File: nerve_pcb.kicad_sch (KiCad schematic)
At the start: 48 parts, among them J1 TC2050-IDC, J2 2171750001, J4 472192001, J5 2x8, J6 2x15, SW1 SPST, SW2 SPST, U1 ld39150dt33-r, U2 STM32F446RET, Y1 8M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

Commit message: Schematic corrections
- Add decoupling caps for sensor ICs
- Fix clock circuits
- Add BNO085 clock jumper
- Minor cleanup
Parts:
- removed Y1: 8M, common:xtal_abm3b-8.000mhz-10-1-u-t, symbol common:abm3b-8.000mhz-10-1-u-t
- removed Y2: 32k768, common:xtal_abs25-32.768khz-6-t, symbol common:abs25-32.768khz-6-t
- added Y1: 8M, common:ecs_ecx-64, symbol common:ecs-80-18-23b-jtn-tr_8mhz
- added Y2: 32k768, common:ecs_ecx-34r, symbol common:ecs-_327-12_5-34r-c-tr_32k768hz
- C12, C13: value 20p -> 26p
- C15, C16: value 1p5 -> 15p
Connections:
- net GND: now also Y1.2, Y1.4
- net GPIO_IMU_P0: now also U2.50 (PA15); no longer U2.40 (PC9)
- net GPIO_IMU_RST: now also U2.40 (PC9); no longer U2.50 (PA15)
- net HSE_OUT: now also Y1.3
- net at C12.1, R11.2: now also Y1.1
- net at C15.1, R12.2: now also Y2.1
- net at C16.1, R13.2: now also Y2.2
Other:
- moved on the sheet: C12, C13, C15, C16, R11

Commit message: Major stackup revision and cleanup
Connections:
- net USART1_RX: now also J6.12 (Pin_12); no longer J6.10 (Pin_10)
- net USART1_TX: now also J6.10 (Pin_10); no longer J6.12 (Pin_12)

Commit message: Fix HSE clock caps
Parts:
- C12, C13: value 26p -> 30p
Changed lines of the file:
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@@
 			)
 		)
-		(property "Value" "26p"
+		(property "Value" "30p"
 			(at 40.64 109.22 0)
 			(effects
@@
 			)
 		)
-		(property "Value" "26p"
+		(property "Value" "30p"
 			(at 22.86 109.22 0)
 			(effects

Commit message: Simplify clock circuits
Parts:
- removed R11, R12, R13: 0R, Resistor_SMD:R_0603_1608Metric, symbol Device:R
- C12, C13: footprint Capacitor_SMD:C_0603_1608Metric -> Capacitor_SMD:C_0402_1005Metric
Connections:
- net HSE_IN: now also C12.1, Y1.1
- net LSE_IN: now also C15.1, Y2.1
- net LSE_OUT: now also C16.1, Y2.2
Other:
- moved on the sheet: C15, C16, Y2

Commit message: Swap 32k768 crystal caps to 18pF
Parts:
- C15, C16: value 15p -> 18p
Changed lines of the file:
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@@
 			)
 		)
-		(property "Value" "15p"
+		(property "Value" "18p"
 			(at 22.86 153.67 0)
 			(effects
@@
 			)
 		)
-		(property "Value" "15p"
+		(property "Value" "18p"
 			(at 40.64 153.67 0)
 			(effects

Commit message: Update J5 2x8 GPS connector
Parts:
- removed J5: 2x8, Connector_PinSocket_1.27mm:PinSocket_2x08_P1.27mm_Vertical_SMD, symbol Connector_Generic:Conn_02x08_Odd_Even
- added J5: BF030-16A-B1-0360-0277-0600-LB, connectors:bf030-16a-b1-0360-0277-0600-lb, symbol connectors:bf030-16a-b1-0360-0277-0600-lb
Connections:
- net +3.3VBATT: now also J5.13
- net +3V3: now also J5.3, J5.4
- net +5V: now also J5.1, J5.2
- net GND: now also J5.12, J5.9
- net GPIO_GPS_RST: now also J5.11
- net PC1: now also J5.6
- net PC2: now also J5.8
- net PC3: now also J5.10
- net TIM1_CH1_PWM: now also J5.14
- net USART2_RX: now also J5.5
- net USART2_TX: now also J5.7
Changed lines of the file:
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@@
-	)
-	(symbol
-		(lib_id "Connector_Generic:Conn_02x08_Odd_Even")
-		(at 195.58 129.54 0)
-		(unit 1)
-		(exclude_from_sim no)
-		(in_bom yes)
-		(on_board yes)
-		(dnp no)
-		(fields_autoplaced yes)
-		(property "Reference" "J5"
-			(at 196.85 115.57 0)
-			(effects
-				(font
-					(size 1.27 1.27)
-				)
-			)
-		)
-		(property "Value" "2x8"
-			(at 196.85 118.11 0)
-			(effects
-				(font
-					(size 1.27 1.27)
-				)
-			)
-		)
-		(property "Footprint" "Connector_PinSocket_1.27mm:PinSocket_2x08_P1.27mm_Vertical_SMD"
-			(at 195.58 129.54 0)
-			(effects
-				(font
-					(size 1.27 1.27)
-				)
-				(hide yes)
-			)
-		)
-		(property "Datasheet" "~"
-			(at 195.58 129.54 0)
-			(effects
-				(font
-					(size 1.27 1.27)
-				)
-				(hide yes)
-			)
-		)
-		(property "Description" "Generic connector, double row, 02x08, odd/even pin numbering scheme (row 1 odd numbers, row 2 even numbers), script generated (kicad-library-utils/schlib/autogen/connector/)"
-			(at 195.58 129.54 0)
-			(effects
-				(font
-					(size 1.27 1.27)
-				)
-				(hide yes)
-			)
-		)
-		(pin "1"
-		)
-		(pin "3"
-		)
-		(pin "7"
-		)
-		(pin "4"
-		)
-		(pin "13"
-		)
-		(pin "14"
-		)
-		(pin "2"
-		)
-		(pin "10"
-		)
-		(pin "6"
-		)
-		(pin "8"
-		)
-		(pin "15"
-		)
-		(pin "11"
-		)
-		(pin "12"
-		)
-		(pin "9"
-		)
-		(pin "5"
-		)
-		(pin "16"
-		)
-		(instances
-			(project ""
-				(path "/c0277862-b3f2-4e0e-986f-34702f0543f0"
-					(reference "J5")
-					(unit 1)
-				)
-			)
-		)
 	)
 	(symbol
@@
 					(unit 1)
 				)
+			)
+		)
+	)
+	(symbol
+		(lib_id "connectors:bf030-16a-b1-0360-0277-0600-lb")
+		(at 196.85 130.81 0)
+		(unit 1)
+		(exclude_from_sim no)
+		(in_bom yes)
+		(on_board yes)
+		(dnp no)
+		(property "Reference" "J5"
+			(at 196.85 119.38 0)
+			(effects
+				(font
+					(size 1.27 1.27)
+				)
+			)
+		)
+		(property "Value" "BF030-16A-B1-0360-0277-0600-LB"
+			(at 196.85 147.32 0)
+			(effects
+				(font
+					(size 1.27 1.27)
+				)
+				(hide yes)
+			)
+		)
+		(property "Footprint" "connectors:bf030-16a-b1-0360-0277-0600-lb"
+			(at 196.85 130.81 0)
+			(effects
+				(font
+					(size 1.27 1.27)
+				)
+				(hide yes)
+			)
+		)
+		(property "Datasheet" "https://gct.co/files/drawings/bf030.pdf"
+			(at 196.85 130.81 0)
+			(effects
+				(font
+					(size 1.27 1.27)
+				)
+				(hide yes)
+			)
+		)
+		(property "Description" "Connector Header Surface Mount 16 position 0.079\" (2.00mm)"
+			(at 196.85 130.81 0)
+			(effects
+				(font
+					(size 1.27 1.27)
+				)
+				(hide yes)
+			)
+		)
+		(property "Manufacturer" "GCT"
+			(at 196.85 130.81 0)
+			(effects
+				(font
+					(size 1.27 1.27)
+				)
+				(hide yes)
+			)
+		)
+		(property "Manufacturer Part Number" "BF030-16A-B1-0360-0277-0600-LB"
+			(at 196.85 130.81 0)
+			(effects
+				(font
+					(size 1.27 1.27)
+				)
+				(hide yes)
+			)
+		)
+		(property "Distributor" "DigiKey"
+			(at 196.85 130.81 0)
+			(effects
+				(font
+					(size 1.27 1.27)
+				)
+				(hide yes)
+			)
+		)
+		(property "Distributor Part Number" "2073-BF030-16A-B1-0360-0277-0600-LBCT-ND"
+			(at 196.85 130.81 0)
+			(effects
+				(font
+					(size 1.27 1.27)
+				)
+				(hide yes)
+			)
+		)
+		(property "Distributor Link" "https://www.digikey.ca/en/products/detail/gct/BF030-16A-B1-0360-0277-0600-LB/16397007"
+			(at 196.85 130.81 0)
+			(effects
+				(font
+					(size 1.27 1.27)
+				)
+				(hide yes)
+			)
+		)
+		(pin "4"
+		)
+		(pin "9"
+		)
+		(pin "13"
+		)
+		(pin "10"
+		)
+		(pin "16"
+		)
+		(pin "8"
+		)
+		(pin "12"
+		)
+		(pin "2"
+		)
+		(pin "7"
+		)
+		(pin "1"
+		)
+		(pin "6"
+		)
+		(pin "15"
+		)
+		(pin "3"
+		)
+		(pin "5"
+		)
+		(pin "11"
+		)
+		(pin "14"
+		)
+		(instances
+			(project ""
+				(path "/c0277862-b3f2-4e0e-986f-34702f0543f0"
+					(reference "J5")
+					(unit 1)
+				)

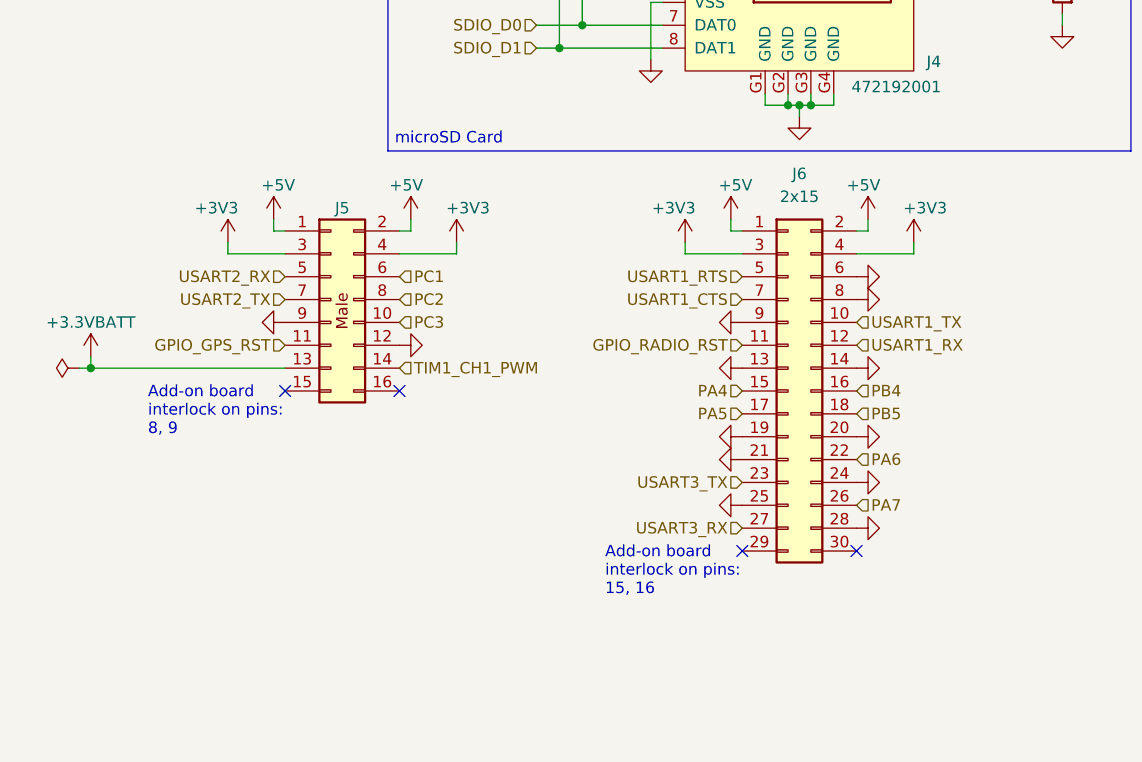
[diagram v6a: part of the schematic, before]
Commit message: Cleanup and update 2x10 Radio connector
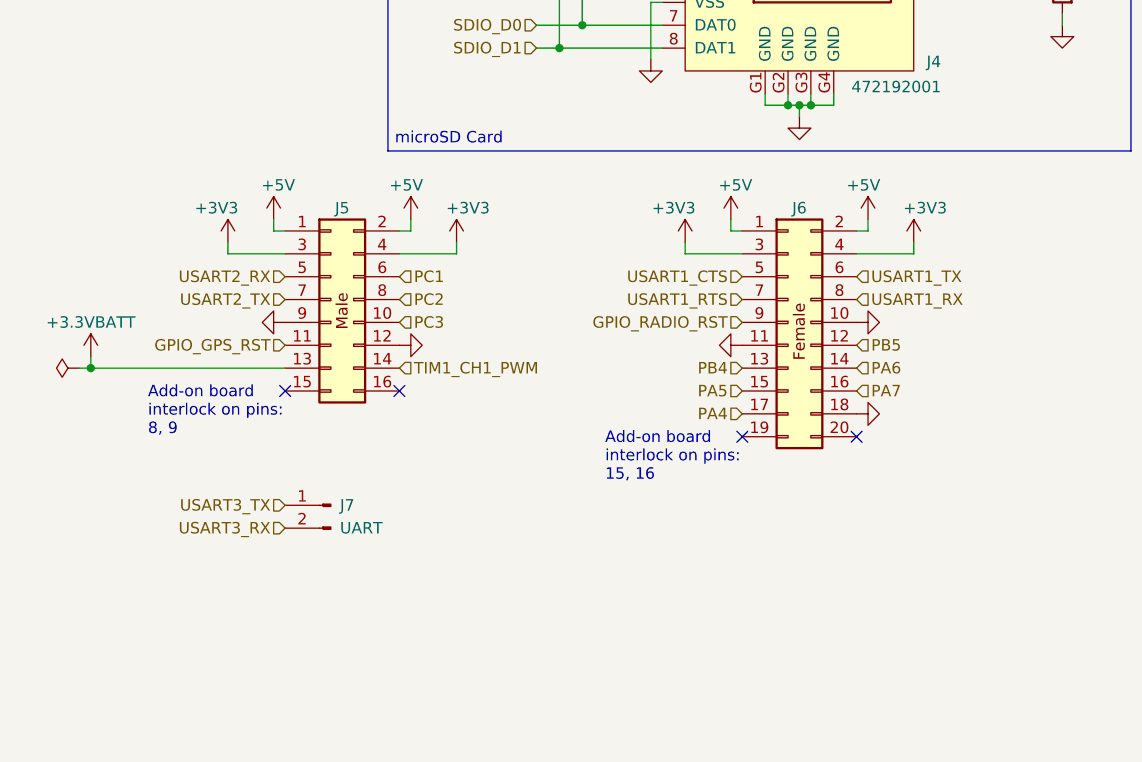
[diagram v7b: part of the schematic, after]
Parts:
- removed J6: 2x15, Connector_PinSocket_1.27mm:PinSocket_2x15_P1.27mm_Vertical_SMD, symbol Connector_Generic:Conn_02x15_Odd_Even
- added J6: BF080-20-A-1-L-C, connectors:bf080-20-a-1-l-c, symbol connectors:bf080-20-a-1-l-c
- added J7: UART, Connector_PinHeader_2.54mm:PinHeader_1x02_P2.54mm_Vertical, symbol Connector:Conn_01x02_Pin
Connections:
- net +3V3: now also J6.3, J6.4
- net +5V: now also J6.1, J6.2
- net GND: now also J6.10, J6.11, J6.18
- net GPIO_RADIO_RST: now also J6.9
- net PA4: now also J6.17
- net PA5: now also J6.15
- net PA6: now also J6.14
- net PA7: now also J6.16
- net PB4: now also J6.13
- net PB5: now also J6.12
- net USART1_CTS: now also J6.5
- net USART1_RTS: now also J6.7
- net USART1_RX: now also J6.8
- net USART1_TX: now also J6.6
- net USART3_RX: now also J7.2 (Pin_2)
- net USART3_TX: now also J7.1 (Pin_1)

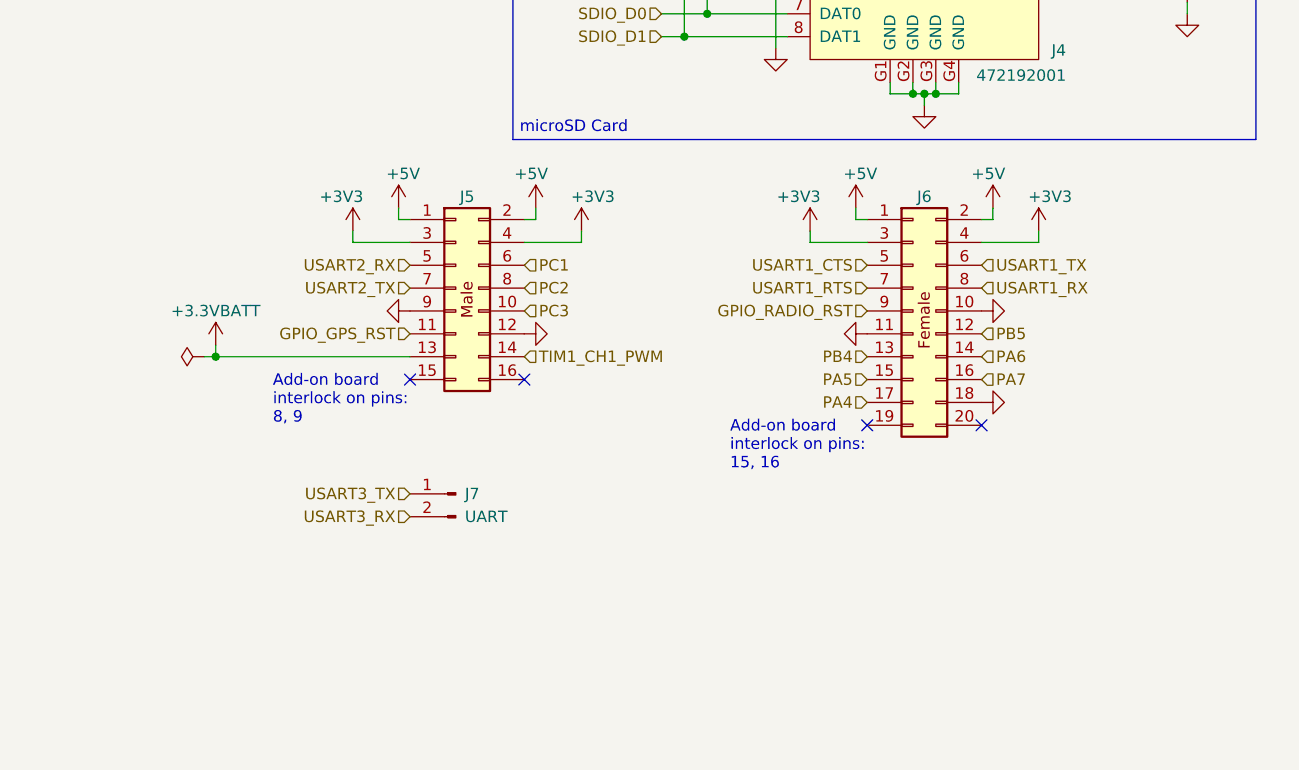
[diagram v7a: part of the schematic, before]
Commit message: Cleanup schematic and change J7 footprint
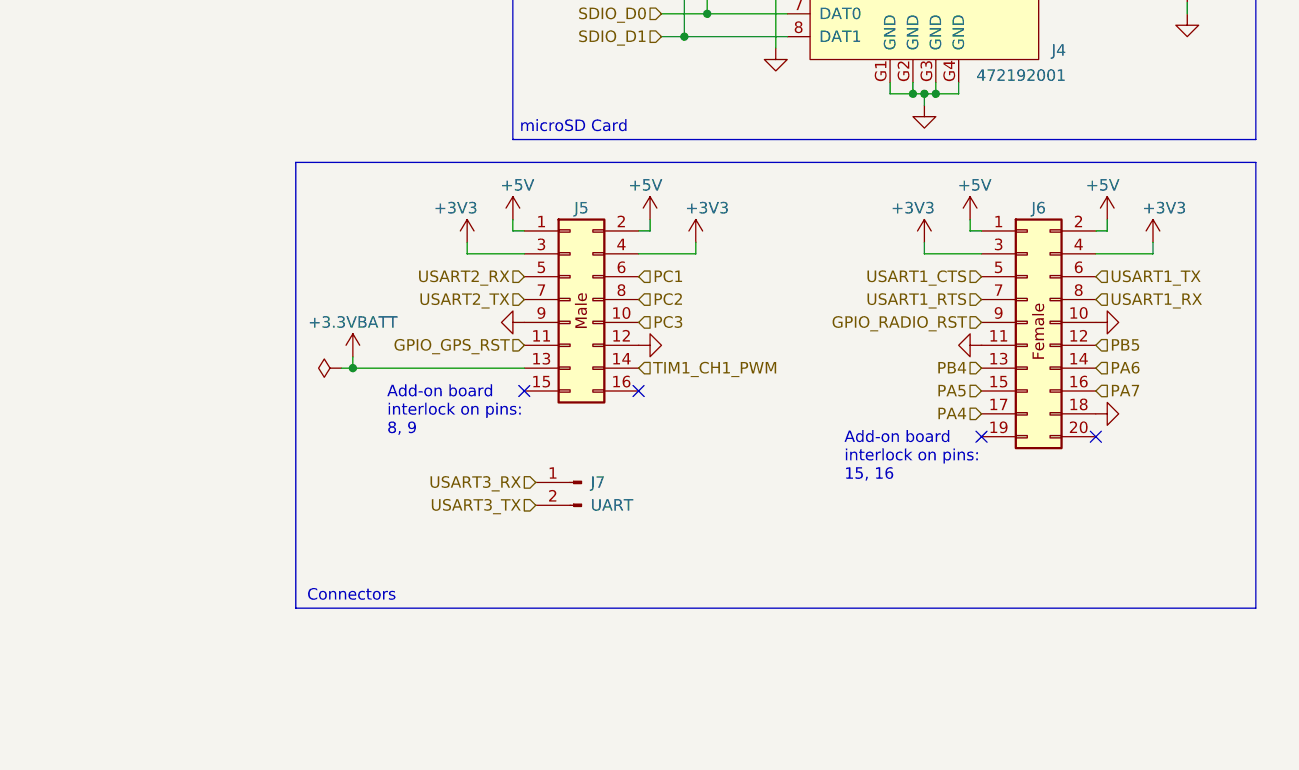
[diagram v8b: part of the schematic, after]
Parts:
- J7: footprint Connector_PinHeader_2.54mm:PinHeader_1x02_P2.54mm_Vertical -> Connector_PinHeader_2.54mm:PinHeader_1x02_P2.54mm_Horizontal
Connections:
- net USART3_RX: now also J7.1 (Pin_1); no longer J7.2 (Pin_2)
- net USART3_TX: now also J7.2 (Pin_2); no longer J7.1 (Pin_1)
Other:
- note added: "Connectors"
- moved on the sheet: J5, J6, J7
